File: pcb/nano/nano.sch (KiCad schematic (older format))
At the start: 4 parts

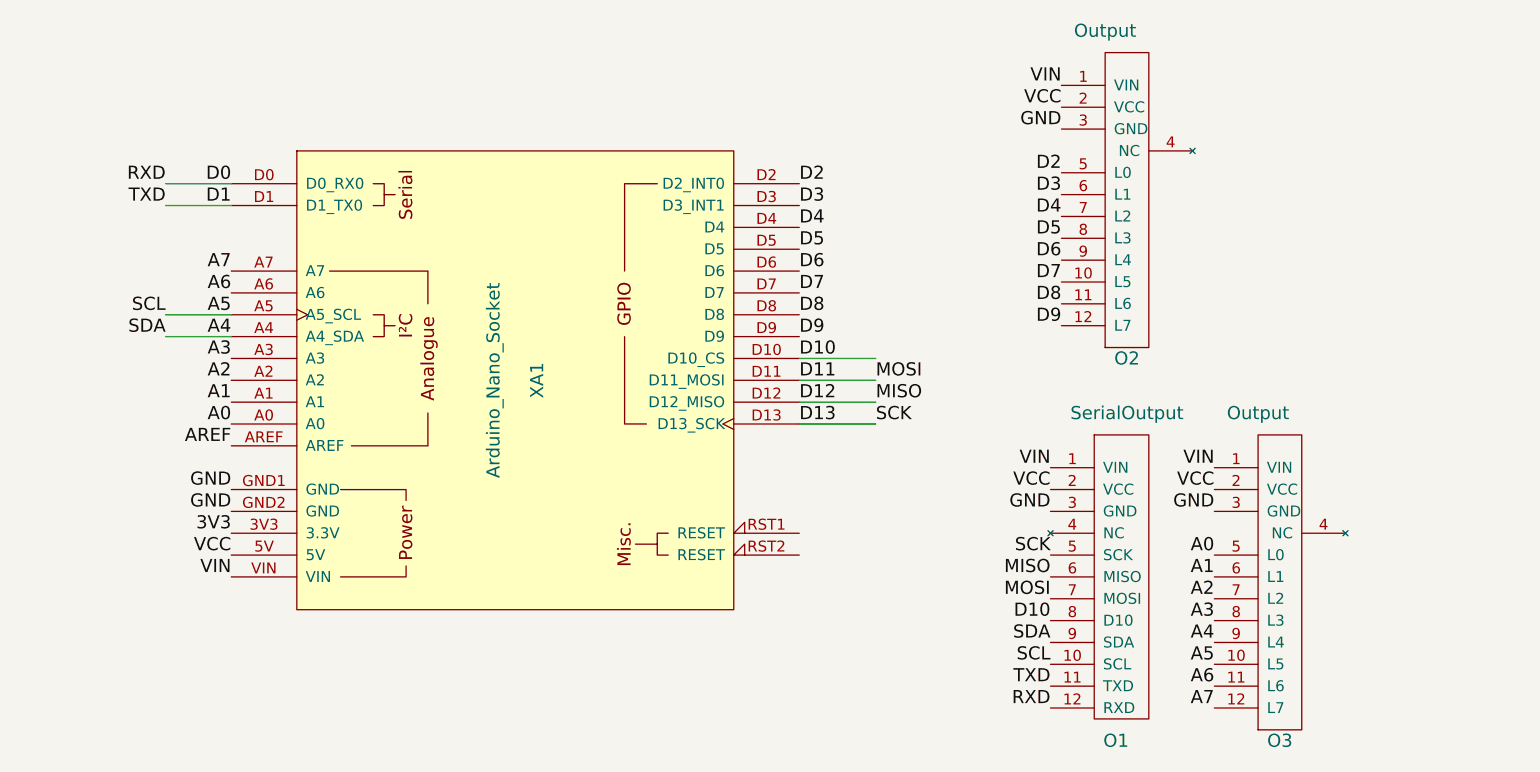
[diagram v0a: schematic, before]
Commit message: Added a Rotary Encoder module. Tidied up a couple of modules before printing them.
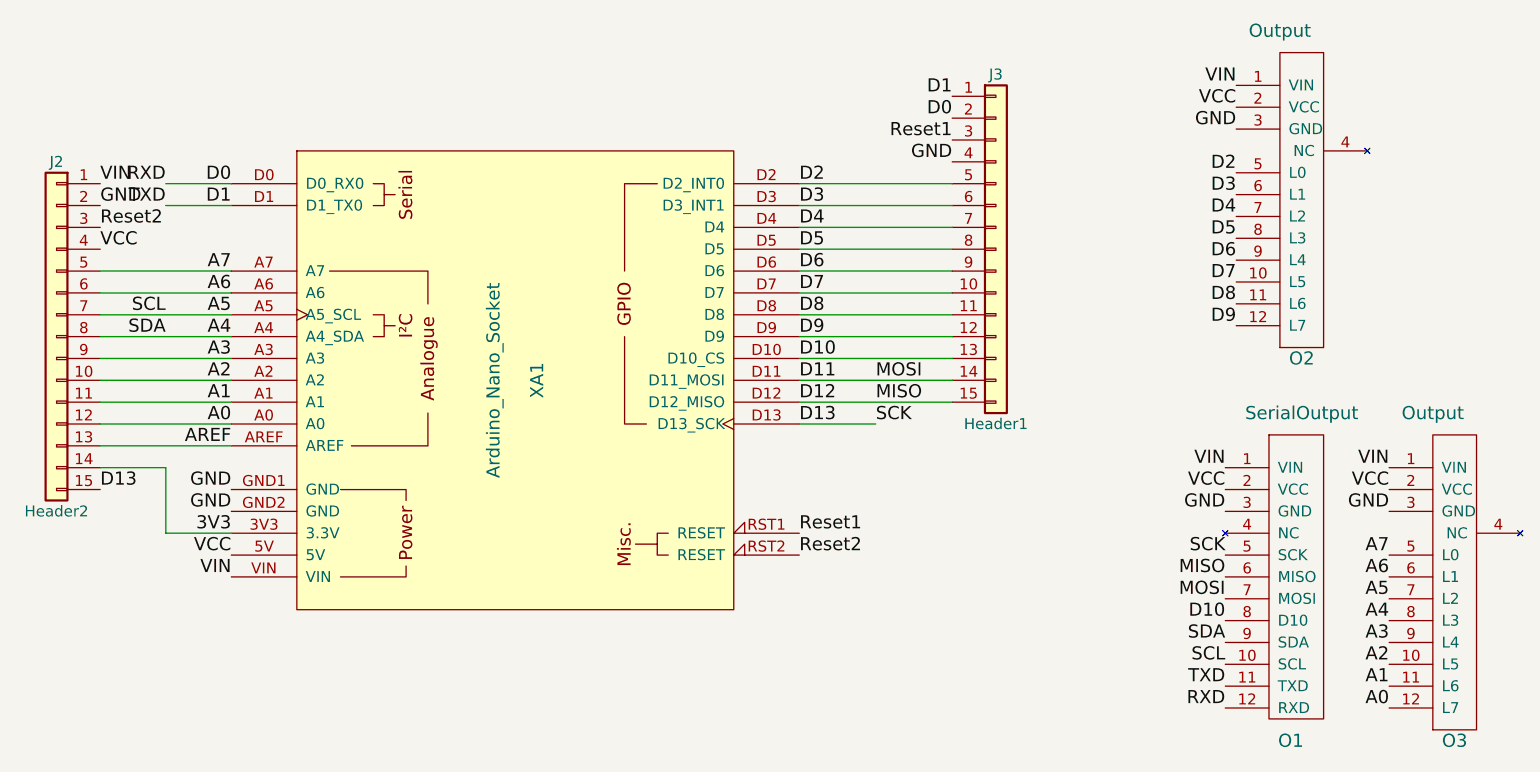
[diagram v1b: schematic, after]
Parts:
- added J2: Header2, Pin_Headers:Pin_Header_Straight_1x15_Pitch2.54mm, symbol Conn_01x15
- added J3: Header1, Pin_Headers:Pin_Header_Straight_1x15_Pitch2.54mm, symbol Conn_01x15
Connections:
- net labels added: Reset1, Reset2
- wire segments 8 -> 26
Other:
- moved on the sheet: O1, O2, O3
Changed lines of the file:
@@
 L Output O2
 U 1 1 5AC3A751
-P 5650 1150
-F 0 "O2" H 5650 -400 60  0000 C CNN
-F 1 "Output" H 5550 1100 60  0000 C CNN
-F 2 "Socket_Strips:Socket_Strip_Straight_1x12_Pitch2.54mm" H 5700 1100 60  0001 C CNN
-F 3 "" H 5700 1100 60  0001 C CNN
-	1    5650 1150
+P 6450 1150
+F 0 "O2" H 6450 -400 60  0000 C CNN
+F 1 "Output" H 6350 1100 60  0000 C CNN
+F 2 "Socket_Strips:Socket_Strip_Straight_1x12_Pitch2.54mm" H 6500 1100 60  0001 C CNN
+F 3 "" H 6500 1100 60  0001 C CNN
+	1    6450 1150
 	1    0    0    -1
 $EndComp
@@
 L SerialOutput O1
 U 1 1 5AC3A80A
-P 5600 2900
-F 0 "O1" H 5600 1350 60  0000 C CNN
-F 1 "SerialOutput" H 5650 2850 60  0000 C CNN
-F 2 "Socket_Strips:Socket_Strip_Straight_1x12_Pitch2.54mm" H 5650 2850 60  0001 C CNN
-F 3 "" H 5650 2850 60  0001 C CNN
-	1    5600 2900
+P 6400 2900
+F 0 "O1" H 6400 1350 60  0000 C CNN
+F 1 "SerialOutput" H 6450 2850 60  0000 C CNN
+F 2 "Socket_Strips:Socket_Strip_Straight_1x12_Pitch2.54mm" H 6450 2850 60  0001 C CNN
+F 3 "" H 6450 2850 60  0001 C CNN
+	1    6400 2900
 	1    0    0    -1
 $EndComp
@@
 L Output O3
 U 1 1 5AC3A8AB
-P 6350 2900
-F 0 "O3" H 6350 1350 60  0000 C CNN
-F 1 "Output" H 6250 2850 60  0000 C CNN
-F 2 "Socket_Strips:Socket_Strip_Straight_1x12_Pitch2.54mm" H 6400 2850 60  0001 C CNN
-F 3 "" H 6400 2850 60  0001 C CNN
-	1    6350 2900
-	1    0    0    -1
-$EndComp
-Text Label 5350 1450 2    60   ~ 0
-VIN
-Text Label 5350 1550 2    60   ~ 0
-VCC
-Text Label 5350 1650 2    60   ~ 0
-GND
-Text Label 5350 1850 2    60   ~ 0
+P 7150 2900
+F 0 "O3" H 7150 1350 60  0000 C CNN
+F 1 "Output" H 7050 2850 60  0000 C CNN
+F 2 "Socket_Strips:Socket_Strip_Straight_1x12_Pitch2.54mm" H 7200 2850 60  0001 C CNN
+F 3 "" H 7200 2850 60  0001 C CNN
+	1    7150 2900
+	1    0    0    -1
+$EndComp
+Text Label 6150 1450 2    60   ~ 0
+VIN
+Text Label 6150 1550 2    60   ~ 0
+VCC
+Text Label 6150 1650 2    60   ~ 0
+GND
+Text Label 6150 1850 2    60   ~ 0
 D2
-Text Label 5350 1950 2    60   ~ 0
+Text Label 6150 1950 2    60   ~ 0
 D3
-Text Label 5350 2050 2    60   ~ 0
+Text Label 6150 2050 2    60   ~ 0
 D4
-Text Label 5350 2150 2    60   ~ 0
+Text Label 6150 2150 2    60   ~ 0
 D5
-Text Label 5350 2250 2    60   ~ 0
+Text Label 6150 2250 2    60   ~ 0
 D6
-Text Label 5350 2350 2    60   ~ 0
+Text Label 6150 2350 2    60   ~ 0
 D7
-Text Label 5350 2450 2    60   ~ 0
+Text Label 6150 2450 2    60   ~ 0
 D8
-Text Label 5350 2550 2    60   ~ 0
+Text Label 6150 2550 2    60   ~ 0
 D9
-Text Label 5300 3200 2    60   ~ 0
-VIN
-Text Label 5300 3300 2    60   ~ 0
-VCC
-Text Label 5300 3400 2    60   ~ 0
-GND
-Text Label 5300 4100 2    60   ~ 0
+Text Label 6100 3200 2    60   ~ 0
+VIN
+Text Label 6100 3300 2    60   ~ 0
+VCC
+Text Label 6100 3400 2    60   ~ 0
+GND
+Text Label 6100 4100 2    60   ~ 0
 SCL
-Text Label 5300 4000 2    60   ~ 0
+Text Label 6100 4000 2    60   ~ 0
 SDA
-Text Label 5300 3600 2    60   ~ 0
+Text Label 6100 3600 2    60   ~ 0
 SCK
-Text Label 5300 3700 2    60   ~ 0
+Text Label 6100 3700 2    60   ~ 0
 MISO
-Text Label 5300 3800 2    60   ~ 0
+Text Label 6100 3800 2    60   ~ 0
 MOSI
-Text Label 5300 3900 2    60   ~ 0
+Text Label 6100 3900 2    60   ~ 0
 D10
-Text Label 5300 4200 2    60   ~ 0
+Text Label 6100 4200 2    60   ~ 0
 TXD
-Text Label 5300 4300 2    60   ~ 0
+Text Label 6100 4300 2    60   ~ 0
 RXD
-Text Label 6050 3200 2    60   ~ 0
-VIN
-Text Label 6050 3300 2    60   ~ 0
-VCC
-Text Label 6050 3400 2    60   ~ 0
-GND
-Text Label 6050 3600 2    60   ~ 0
+Text Label 6850 3200 2    60   ~ 0
+VIN
+Text Label 6850 3300 2    60   ~ 0
+VCC
+Text Label 6850 3400 2    60   ~ 0
+GND
+Text Label 6850 4300 2    60   ~ 0
 A0
-Text Label 6050 3700 2    60   ~ 0
+Text Label 6850 4200 2    60   ~ 0
 A1
-Text Label 6050 3800 2    60   ~ 0
+Text Label 6850 4100 2    60   ~ 0
 A2
-Text Label 6050 3900 2    60   ~ 0
+Text Label 6850 4000 2    60   ~ 0
 A3
-Text Label 6050 4000 2    60   ~ 0
+Text Label 6850 3900 2    60   ~ 0
 A4
-Text Label 6050 4100 2    60   ~ 0
+Text Label 6850 3800 2    60   ~ 0
 A5
 $Comp
@@
 Text Label 4150 3000 0    60   ~ 0
 D13
-Wire Wire Line
-	4150 2700 4500 2700
-Wire Wire Line
-	4150 2800 4500 2800
-Wire Wire Line
-	4150 2900 4500 2900
-Wire Wire Line
-	4150 3000 4500 3000
 Text Label 4500 2800 0    60   ~ 0
 MOSI
@@
 Text Label 1550 3100 2    60   ~ 0
 AREF
-Wire Wire Line
-	1550 1900 1250 1900
-Wire Wire Line
-	1550 2000 1250 2000
 Text Label 1250 1900 2    60   ~ 0
 RXD
 Text Label 1250 2000 2    60   ~ 0
 TXD
-Wire Wire Line
-	1550 2500 1250 2500
-Wire Wire Line
-	1550 2600 1250 2600
 Text Label 1250 2500 2    60   ~ 0
 SCL
 Text Label 1250 2600 2    60   ~ 0
 SDA
-Text Label 6050 4200 2    60   ~ 0
+Text Label 6850 3700 2    60   ~ 0
 A6
-Text Label 6050 4300 2    60   ~ 0
+Text Label 6850 3600 2    60   ~ 0
 A7
+Text Label 4150 3500 0    60   ~ 0
+Reset1
+$Comp
+L Conn_01x15 J3
+U 1 1 5AE971FE
+P 5050 2200
+F 0 "J3" H 5050 3000 50  0000 C CNN
+F 1 "Header1" H 5050 1400 50  0000 C CNN
+F 2 "Pin_Headers:Pin_Header_Straight_1x15_Pitch2.54mm" H 5050 2200 50  0001 C CNN
+F 3 "" H 5050 2200 50  0001 C CNN
+	1    5050 2200
+	1    0    0    -1
+$EndComp
+Text Label 4850 1800 2    60   ~ 0
+GND
+Text Label 4850 1700 2    60   ~ 0
+Reset1
+Text Label 4150 3600 0    60   ~ 0
+Reset2
+Text Label 4850 1500 2    60   ~ 0
+D1
+Text Label 4850 1600 2    60   ~ 0
+D0
+$Comp
+L Conn_01x15 J2
+U 1 1 5AE97778
+P 750 2600
+F 0 "J2" H 750 3400 50  0000 C CNN
+F 1 "Header2" H 750 1800 50  0000 C CNN
+F 2 "Pin_Headers:Pin_Header_Straight_1x15_Pitch2.54mm" H 750 2600 50  0001 C CNN
+F 3 "" H 750 2600 50  0001 C CNN
+	1    750  2600
+	-1   0    0    -1
+$EndComp
+Wire Wire Line
+	4150 2700 4850 2700
+Wire Wire Line
+	4150 2800 4850 2800
+Wire Wire Line
+	4150 2900 4850 2900
+Wire Wire Line
+	4150 3000 4500 3000
+Wire Wire Line
+	1550 1900 1250 1900
+Wire Wire Line
+	1550 2000 1250 2000
+Wire Wire Line
+	950  2500 1550 2500
+Wire Wire Line
+	950  2600 1550 2600
+Wire Wire Line
+	4850 2600 4150 2600
+Wire Wire Line
+	4150 2500 4850 2500
+Wire Wire Line
+	4850 2400 4150 2400
+Wire Wire Line
+	4150 2300 4850 2300
+Wire Wire Line
+	4850 2200 4150 2200
+Wire Wire Line
+	4150 2100 4850 2100
+Wire Wire Line
+	4850 2000 4150 2000
+Wire Wire Line
+	4150 1900 4850 1900
+Wire Wire Line
+	1550 2300 950  2300
+Wire Wire Line
+	1550 2400 950  2400
+Wire Wire Line
+	1550 2700 950  2700
+Wire Wire Line
+	950  2800 1550 2800
+Wire Wire Line
+	1550 2900 950  2900
+Wire Wire Line
+	950  3000 1550 3000
+Wire Wire Line
+	1550 3100 950  3100
+Wire Wire Line
+	1550 3500 1250 3500
+Wire Wire Line
+	1250 3500 1250 3200
+Wire Wire Line
+	1250 3200 950  3200
+Text Label 950  3300 0    60   ~ 0
+D13
+Text Label 950  2200 0    60   ~ 0
+VCC
+Text Label 950  2100 0    60   ~ 0
+Reset2
+Text Label 950  2000 0    60   ~ 0
+GND
+Text Label 950  1900 0    60   ~ 0
+VIN
 $EndSCHEMATC
